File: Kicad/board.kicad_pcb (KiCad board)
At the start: 2 copper layers, 100 x 91.4 mm, 32 parts, among them SW1 SW_Push, SW10 SW_Push, SW11 SW_Push, SW12 SW_Push, SW13 RotaryEncoder, SW2 SW_Push, SW3 SW_Push, SW4 SW_Push, SW5 SW_Push, SW6 SW_Push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

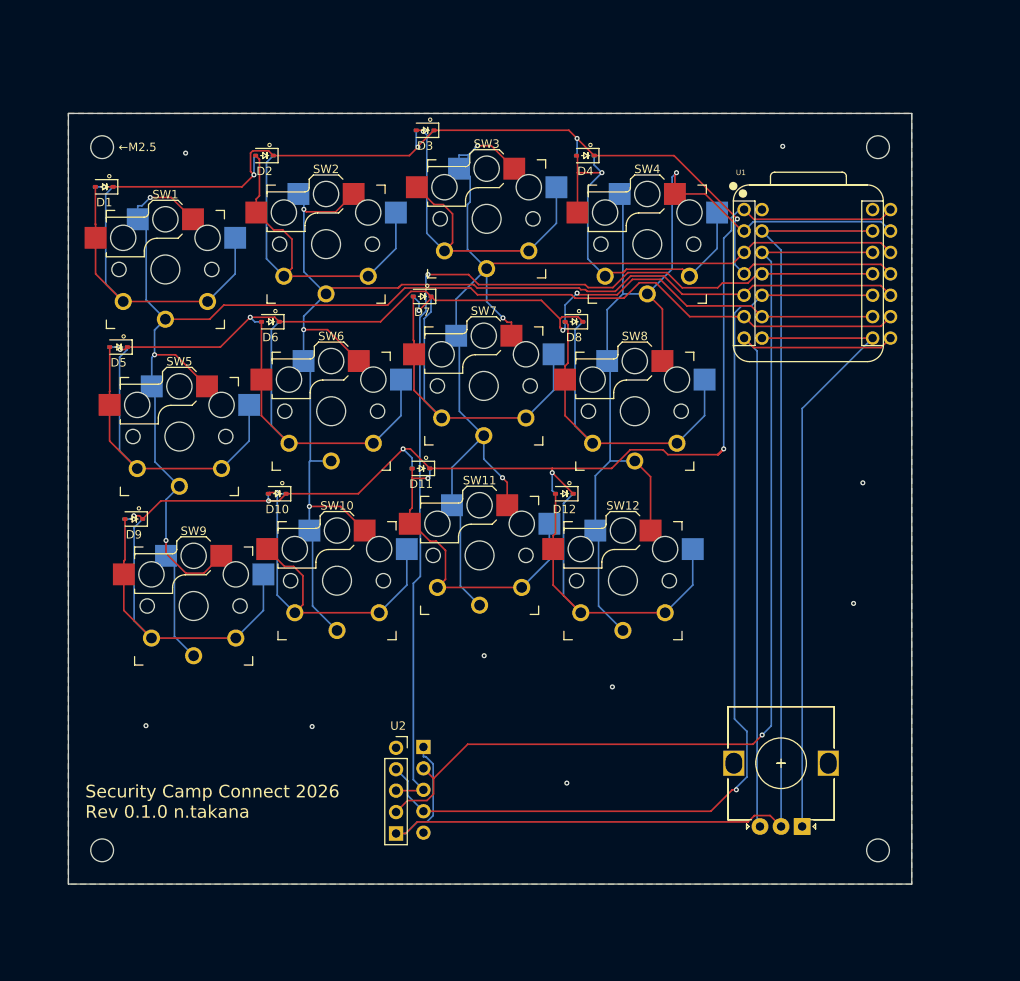
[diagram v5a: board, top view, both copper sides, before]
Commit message: [add] place parts in pcb editor
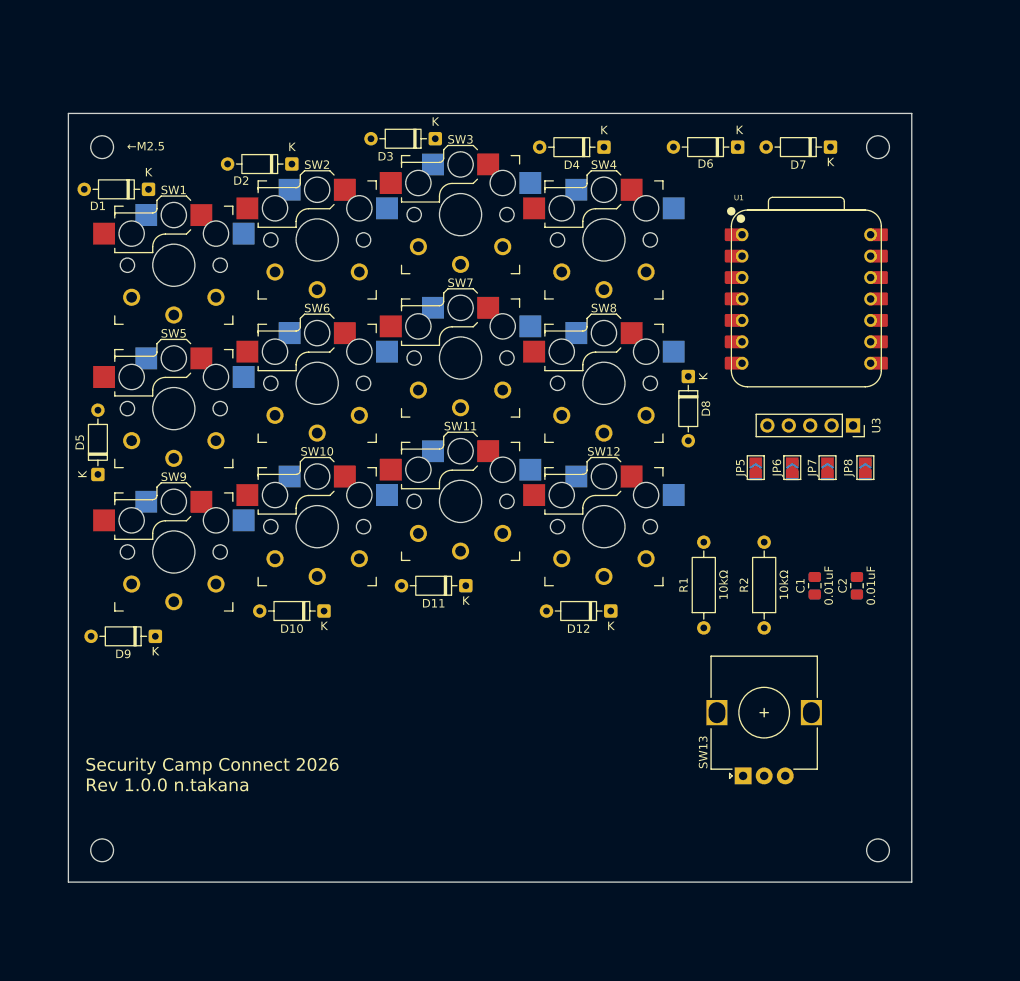
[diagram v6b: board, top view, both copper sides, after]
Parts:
- removed U2: KY-023, ky-023:KY-023
- added C1: 0.01uF, mylib:C_0805_2012_HandSolder_reversible, F.Cu at (147.4, 88.6)
- added C2: 0.01uF, mylib:C_0805_2012_HandSolder_reversible, F.Cu at (152.4, 88.6)
- added JP1: GND, Jumper:SolderJumper-2_P1.3mm_Open_TrianglePad1.0x1.5mm, B.Cu at (153.4, 74.9)
- added JP2: VCC, Jumper:SolderJumper-2_P1.3mm_Open_TrianglePad1.0x1.5mm, B.Cu at (148.9, 74.9)
- added JP3: SCL, Jumper:SolderJumper-2_P1.3mm_Open_TrianglePad1.0x1.5mm, B.Cu at (144.8, 74.9)
- added JP4: SDA, Jumper:SolderJumper-2_P1.3mm_Open_TrianglePad1.0x1.5mm, B.Cu at (140.4, 74.9)
- added JP5: GND, Jumper:SolderJumper-2_P1.3mm_Open_TrianglePad1.0x1.5mm, F.Cu at (140.4, 74.6)
- added JP6: VCC, Jumper:SolderJumper-2_P1.3mm_Open_TrianglePad1.0x1.5mm, F.Cu at (144.8, 74.6)
- added JP7: SCL, Jumper:SolderJumper-2_P1.3mm_Open_TrianglePad1.0x1.5mm, F.Cu at (148.9, 74.6)
- added JP8: SDA, Jumper:SolderJumper-2_P1.3mm_Open_TrianglePad1.0x1.5mm, F.Cu at (153.4, 74.6)
- added R1: 10kΩ, mylib:R_L6.3mm_D2.5mm_P10.16mm_Horizontal_reversible, F.Cu at (134.3, 93.6)
- added R2: 10kΩ, mylib:R_L6.3mm_D2.5mm_P10.16mm_Horizontal_reversible, F.Cu at (141.4, 93.6)
- D1, D10, D11, D12, D2, D3, D4, D5, D6, D7, D8, D9: value 1N4148WS -> 1N4148; footprint mylib:1n4148ws_reversible -> mylib:Diode_THT_reversible
- SW1, SW10, SW11, SW12, SW2, SW3, SW4, SW5, SW6, SW7, SW8, SW9: footprint keyswitches:Kailh_socket_PG1350_optional_reversible -> mylib:Kailh_socket_PG1350_optional_reversible
- SW13: moved to F.Cu
- U3: value KY-023 -> OLED; footprint ky-023:KY-023 -> Connector_PinSocket_2.54mm:PinSocket_1x05_P2.54mm_Vertical; moved to F.Cu
- moved U3 71.5 mm to (152.0, 69.6), turned to -90 degrees
- moved D6 59.2 mm to (138.3, 36.6)
- moved D7 51.5 mm to (149.3, 36.6)
- moved D5 15.3 mm to (62.4, 75.4), turned to 90 degrees
- moved D8 15.0 mm to (132.4, 63.8), turned to -90 degrees
- moved D10 15.0 mm to (89.2, 91.6)
- moved D12 15.0 mm to (123.2, 91.6)
- moved D11 14.9 mm to (106.1, 88.6)
- moved D9 14.1 mm to (69.2, 94.6)
- moved SW13 9.22 mm to (138.9, 111.2)
- moved SW10 6.82 mm to (88.4, 81.6)
- moved SW9 6.82 mm to (71.4, 84.6)
- moved SW11 6.79 mm to (105.4, 78.6)
- moved SW12 6.79 mm to (122.4, 81.6)
- moved D1 5.26 mm to (68.4, 41.6)
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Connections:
- U1 pad 10: joystick_y -> column1
- U1 pad 11: joystick_x -> column2
- U1 pad 12: VCC -> unconnected-(U1-VCC_3V3-Pad12)_1
- U1 pad 14: unconnected-(U1-VBUS-Pad14) -> VCC
- U1 pad 5: column2 -> oled_sda
- U1 pad 6: column1 -> oled_scl
- U3 pad 1: unconnected-(U3-Button-Pad1) -> Net-(JP1-A)
- U3 pad 2: joystick_y -> Net-(JP2-A)
- U3 pad 3: joystick_x -> VCC
- U3 pad 4: VCC -> Net-(JP3-A)
- U3 pad 5: GNDPWR -> Net-(JP4-A)
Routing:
- net column1: track 175.8 -> 0.00 mm, vias 3 -> 0
- net column2: track 151.8 -> 0.00 mm, vias 3 -> 0
- net GNDPWR: track 145.8 -> 0.00 mm, vias 9 -> 0
- net row3: track 139.3 -> 0.00 mm, vias 5 -> 0
- net column3: track 138.5 -> 0.00 mm, vias 3 -> 0
- net column4: track 125.2 -> 0.00 mm, vias 1 -> 0
- net VCC: track 121.2 -> 0.00 mm, vias 1 -> 0
- net joystick_x: track 121.2 -> 0.00 mm, vias 1 -> 0
- net joystick_y: track 119.4 -> 0.00 mm, vias 1 -> 0
- net row1: track 117.7 -> 0.00 mm, vias 5 -> 0
- net row2: track 113.1 -> 0.00 mm, vias 5 -> 0
- net rotary_encoder_b: track 77.0 -> 0.00 mm
- net rotary_encoder_a: track 74.5 -> 0.00 mm
- net Net-(D2-A): track 51.8 -> 0.00 mm
- net Net-(D8-A): track 50.6 -> 0.00 mm
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- removed copper zone on B.Cu, net GNDPWR
- removed copper zone on F.Cu, net GNDPWR
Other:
- board size 100 x 91.4 mm -> 100 x 91.1 mm
- board text added: "Security Camp Connect 2026 Rev 1.0.0 n.takana"
- board text added: "←M2.5"
- board text removed: "Security Camp Connect 2026 Rev 0.1.0 n.takana"

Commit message: [update] update silk and parts placement
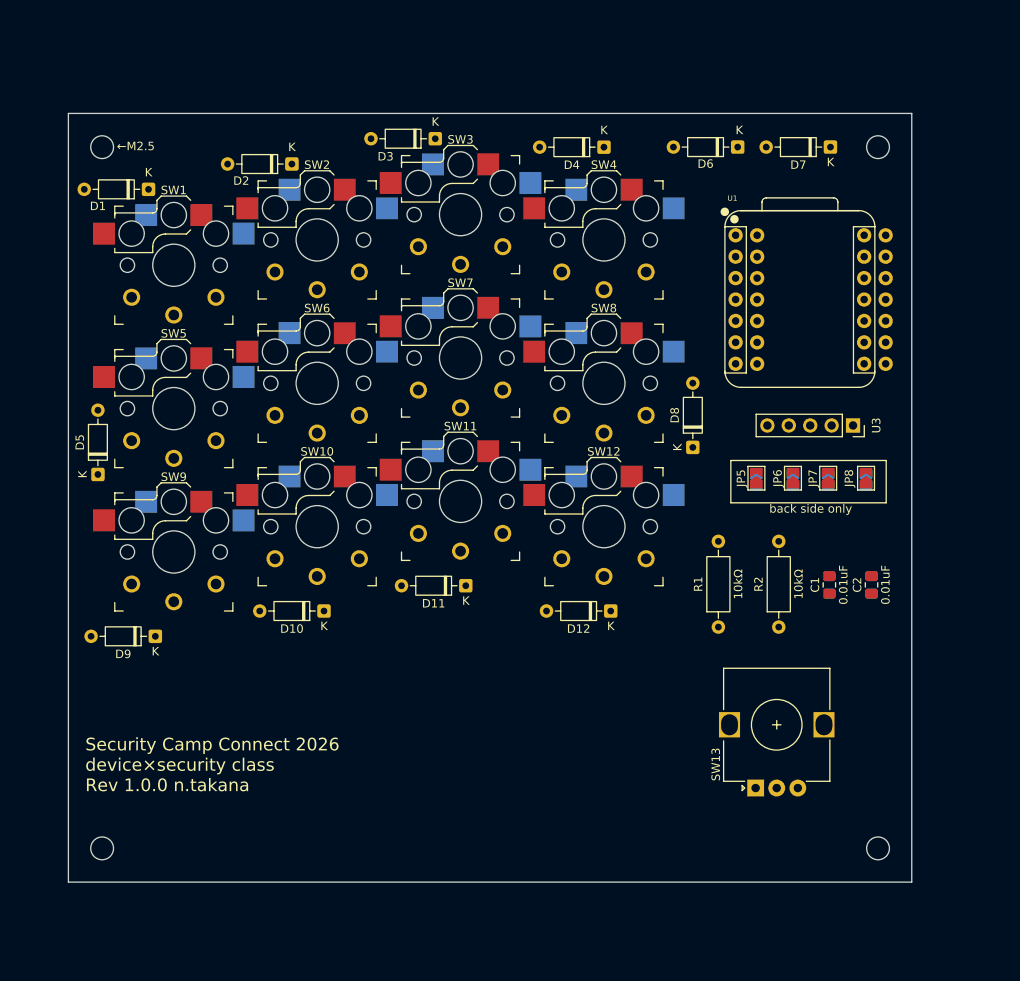
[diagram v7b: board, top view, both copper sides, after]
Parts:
- U1: footprint XIAO-ESP32S3-DIP:XIAO-ESP32S3-DIP -> mylib:XIAO-ESP32S3_reversible
- moved D8 8.43 mm to (133.0, 72.2), turned to 90 degrees
- moved SW13 2.07 mm to (140.4, 112.6)
- moved C1 1.73 mm to (149.2, 88.5)
- moved C2 1.73 mm to (154.2, 88.5)
- moved R1 1.73 mm to (136.0, 93.5)
- moved R2 1.73 mm to (143.2, 93.5)
- moved JP1 1.25 mm to (153.5, 76.2)
- moved JP2 1.25 mm to (149.0, 76.2)
- moved JP3 1.25 mm to (144.9, 76.2)
- moved JP4 1.25 mm to (140.5, 76.2)
- moved JP5 1.25 mm to (140.5, 75.9)
- moved JP6 1.25 mm to (144.9, 75.9)
- moved JP7 1.25 mm to (149.0, 75.9)
- moved JP8 1.25 mm to (153.5, 75.9)
- moved U1 0.77 mm to (145.7, 54.7)
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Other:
- board text added: "Security Camp Connect 2026 device×security class Rev 1.0.0 n.takana"
- board text added: "back side only"
- board text removed: "Security Camp Connect 2026 Rev 1.0.0 n.takana"

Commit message: [!][fix] fix power line connection
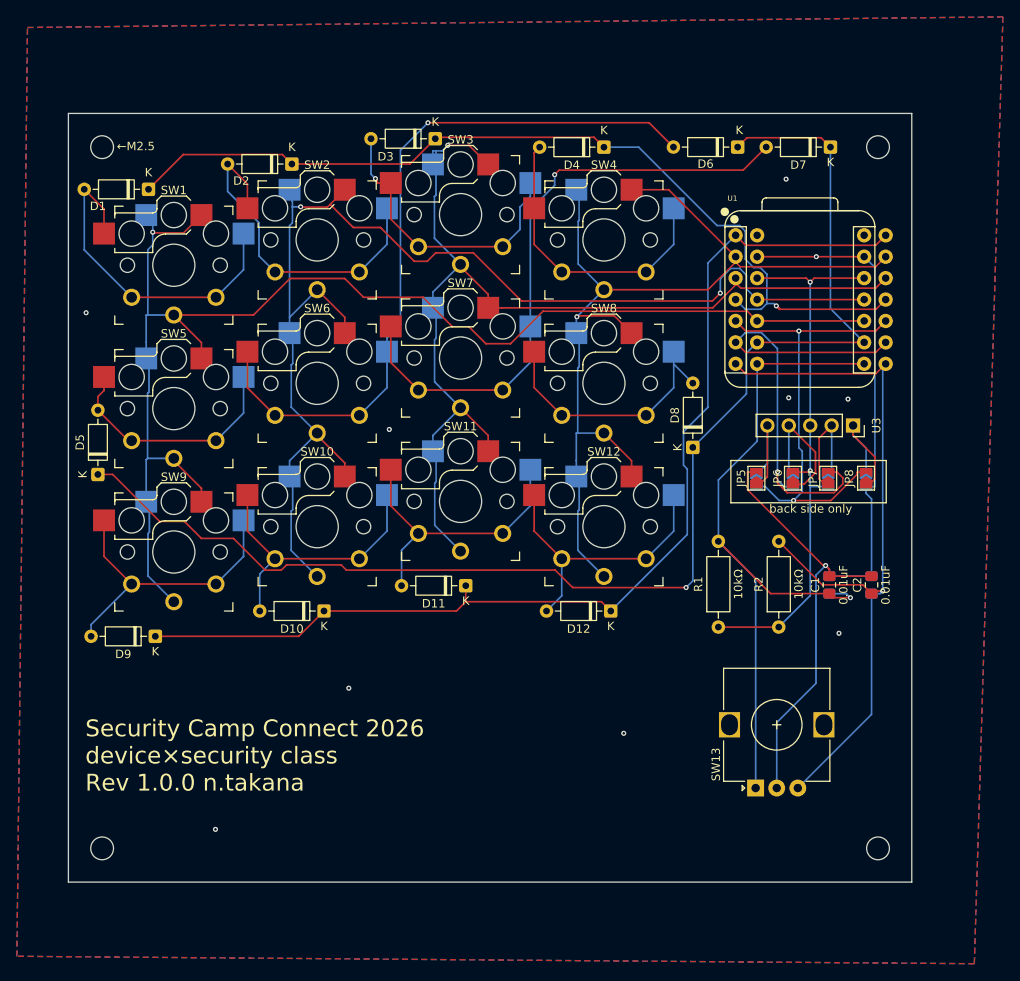
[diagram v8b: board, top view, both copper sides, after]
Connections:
- JP3 pad 2: OLED_SCL -> oled_scl
- JP4 pad 2: OLED_SDA -> oled_sda
- JP7 pad 2: OLED_SCL -> oled_scl
- JP8 pad 2: OLED_SDA -> oled_sda
- U1 pad 12: unconnected-(U1-VCC_3V3-Pad12) -> VCC
- U1 pad 14: VCC -> unconnected-(U1-VBUS-Pad14)
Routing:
- net column1: track 0.00 -> 163.2 mm, vias 0 -> 1
- net row2: track 0.00 -> 157.8 mm, vias 0 -> 1
- net column2: track 0.00 -> 149.4 mm, vias 0 -> 2
- net row3: track 0.00 -> 127.9 mm
- net column3: track 0.00 -> 126.7 mm, vias 0 -> 1
- net column4: track 0.00 -> 119.3 mm, vias 0 -> 1
- net row1: track 0.00 -> 110.5 mm, vias 0 -> 1
- net GNDPWR: track 0.00 -> 110.2 mm, vias 0 -> 11
- net rotary_encoder_b: track 0.00 -> 89.0 mm, vias 0 -> 1
- net rotary_encoder_a: track 0.00 -> 87.8 mm, vias 0 -> 1
- net Net-(D6-A): track 0.00 -> 87.3 mm, vias 0 -> 1
- net Net-(D7-A): track 0.00 -> 73.4 mm, vias 0 -> 1
- net VCC: track 0.00 -> 66.9 mm, vias 0 -> 2
- net oled_scl: track 0.00 -> 55.7 mm, vias 0 -> 1
- net oled_sda: track 0.00 -> 54.7 mm, vias 0 -> 2
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- added copper zone on B.Cu, net GNDPWR
- added copper zone on F.Cu, net GNDPWR
